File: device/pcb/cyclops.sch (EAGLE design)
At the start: 199 parts, among them Q1 NDS351AN, Q2 NDS351AN, Q3 NDS351AN, Q4 IRF510, U1 MCP4921, U10 LT1880, U11 ZXTD, U12 ADG1201, U13 THS4281, U14 ZXTD, U16 OPA1664, U2 LT1764A, U3 BD00FC0WEFJ, U4 LTM8020, U5 LT1931, U6 TPS72325, U7 TLV3701, U75 TXB0104RGYR, U8 LT1711, U9 ADR03

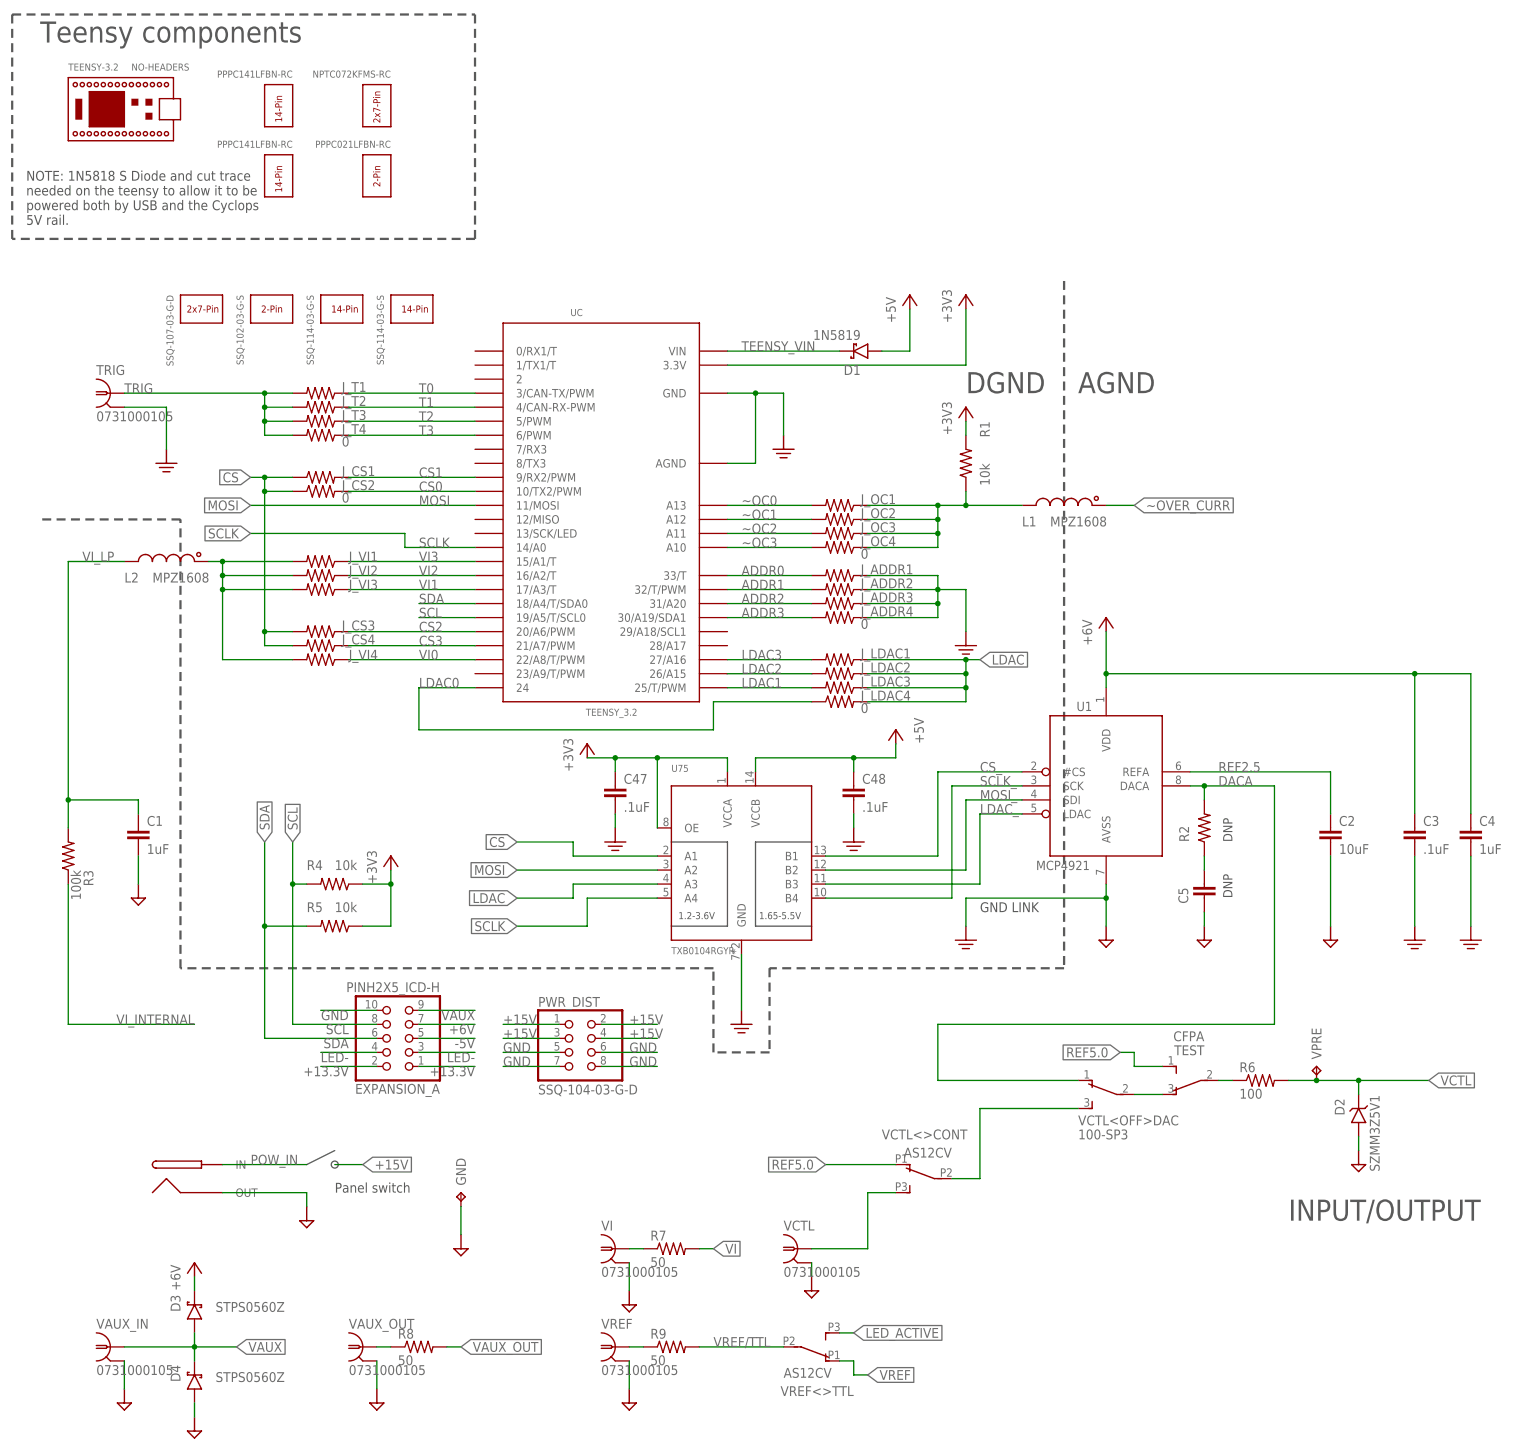
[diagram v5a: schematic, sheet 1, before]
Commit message: More pre-production fixes for Filipe.
- Better cutouts on Exapansion B in panel
- Panel alignment
- Schematic fixes (remove teensy cut trace/diode requirement)
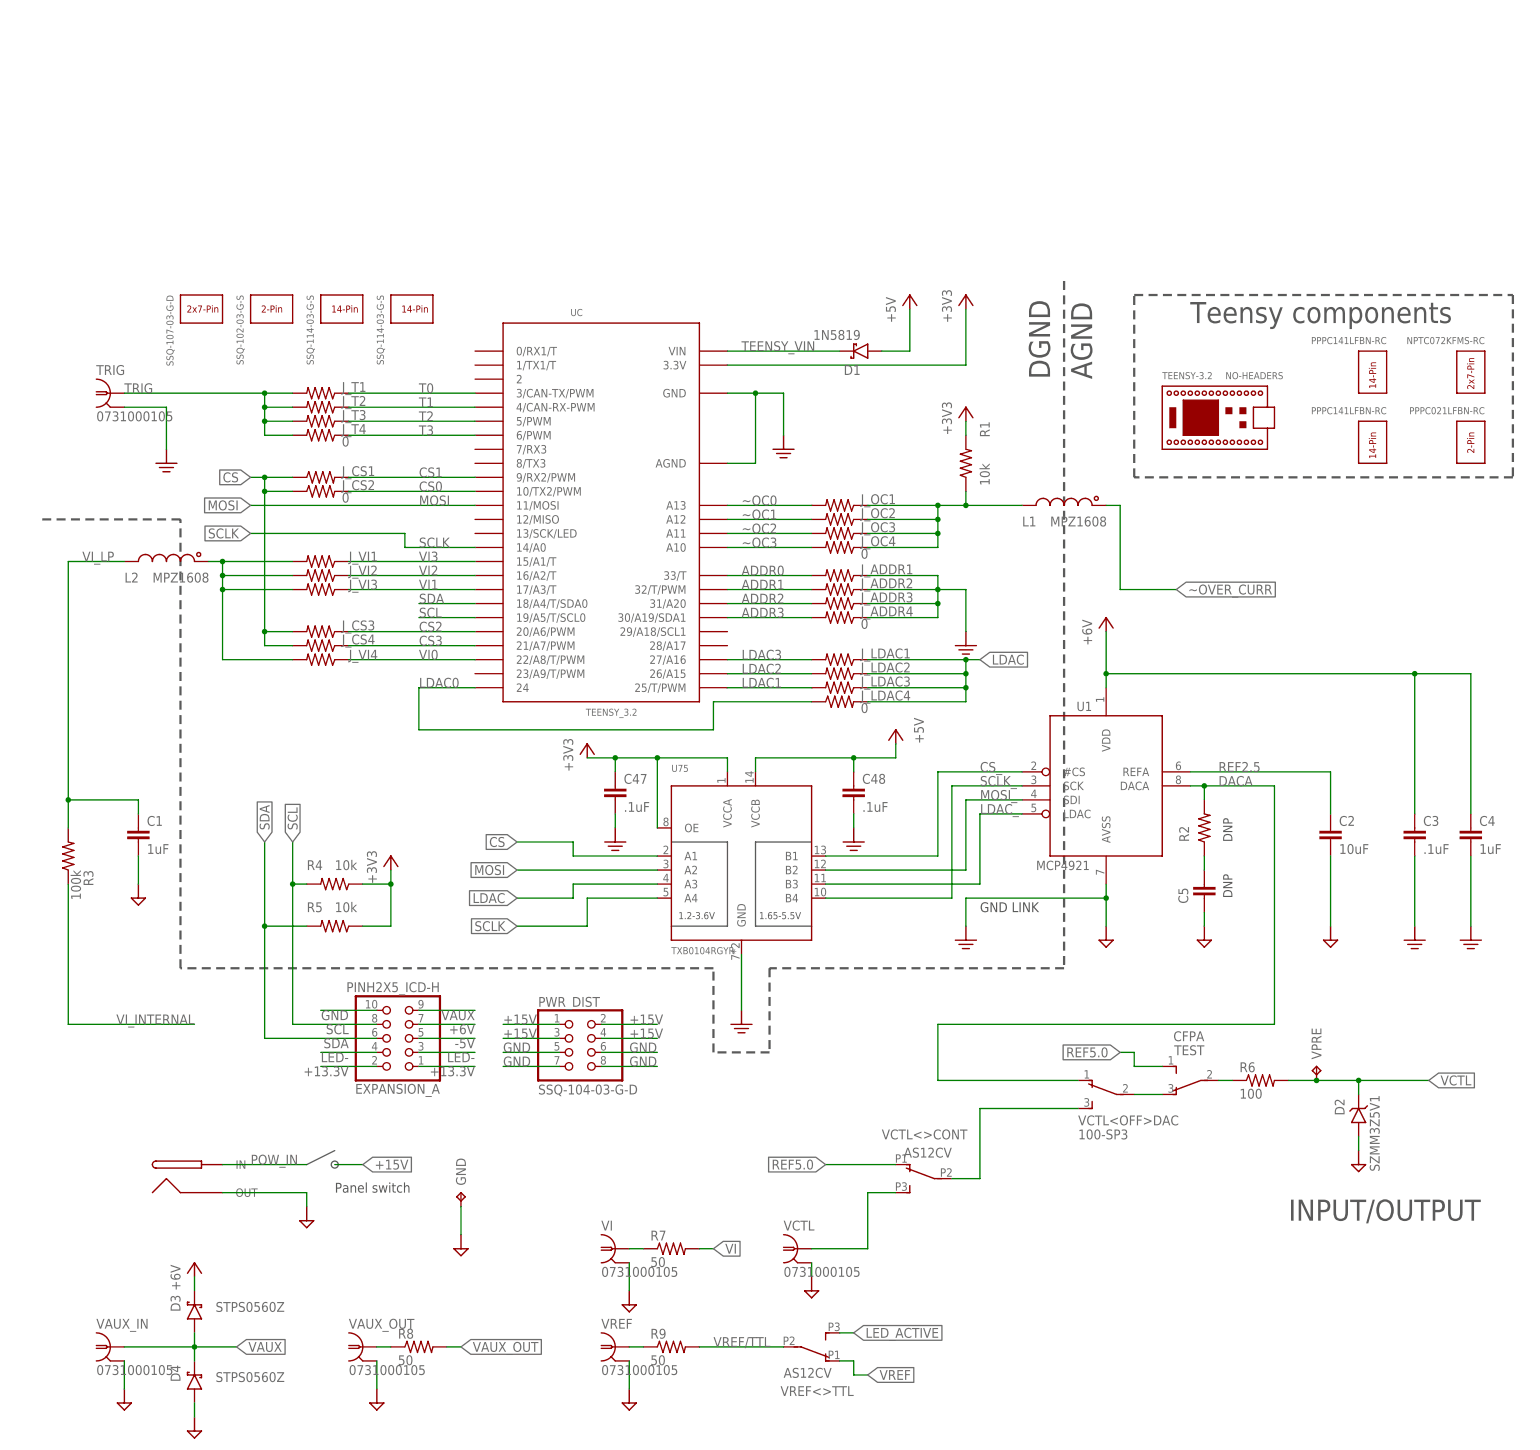
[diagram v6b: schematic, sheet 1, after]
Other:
- note removed: "NOTE: 1N5818 S Diode and cut trace needed on the teensy to allow it to be powered both by USB and the Cyclops 5V rail."
- moved on the sheet: TEENSY-3.2
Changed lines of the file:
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@@
 <wire x1="114.3" y1="2.54" x2="114.3" y2="17.78" width="0.4064" layer="97" style="shortdash"/>
 <wire x1="114.3" y1="17.78" x2="17.78" y2="17.78" width="0.4064" layer="97" style="shortdash"/>
-<text x="180.34" y="121.92" size="3.81" layer="97">AGND</text>
-<text x="160.02" y="121.92" size="3.81" layer="97">DGND</text>
+<text x="182.88" y="124.46" size="3.81" layer="97" rot="R90">AGND</text>
+<text x="175.26" y="124.46" size="3.81" layer="97" rot="R90">DGND</text>
 <wire x1="17.78" y1="17.78" x2="17.78" y2="99.06" width="0.4064" layer="97" style="shortdash"/>
 <wire x1="17.78" y1="99.06" x2="-7.62" y2="99.06" width="0.4064" layer="97" style="shortdash"/>
-<wire x1="-12.7" y1="190.5" x2="71.12" y2="190.5" width="0.4064" layer="97" style="shortdash"/>
-<wire x1="71.12" y1="190.5" x2="71.12" y2="149.86" width="0.4064" layer="97" style="shortdash"/>
-<wire x1="71.12" y1="149.86" x2="-12.7" y2="149.86" width="0.4064" layer="97" style="shortdash"/>
-<wire x1="-12.7" y1="149.86" x2="-12.7" y2="190.5" width="0.4064" layer="97" style="shortdash"/>
-<text x="-7.62" y="185.42" size="3.81" layer="97">Teensy components</text>
+<wire x1="190.5" y1="139.7" x2="259.08" y2="139.7" width="0.4064" layer="97" style="shortdash"/>
+<wire x1="259.08" y1="139.7" x2="259.08" y2="106.68" width="0.4064" layer="97" style="shortdash"/>
+<wire x1="259.08" y1="106.68" x2="190.5" y2="106.68" width="0.4064" layer="97" style="shortdash"/>
+<wire x1="190.5" y1="106.68" x2="190.5" y2="139.7" width="0.4064" layer="97" style="shortdash"/>
+<text x="200.66" y="134.62" size="3.81" layer="97">Teensy components</text>
 <text x="208.28" y="40.64" size="1.6764" layer="97" rot="R90">DNP</text>
 <text x="208.28" y="30.48" size="1.6764" layer="97" rot="R90">DNP</text>
-<text x="-10.16" y="152.4" size="1.778" layer="97">NOTE: 1N5818 S Diode and cut trace
-needed on the teensy to allow it to be
-powered both by USB and the Cyclops
-5V rail.</text>
 </plain>
 <instances>
@@
 <instance part="U$55" gate="G$1" x="43.18" y="134.62"/>
 <instance part="U$63" gate="G$1" x="55.88" y="134.62"/>
-<instance part="U$66" gate="G$1" x="50.8" y="177.8" rot="R270"/>
-<instance part="U$72" gate="G$1" x="33.02" y="177.8" rot="R270"/>
-<instance part="U$73" gate="G$1" x="33.02" y="165.1" rot="R270"/>
-<instance part="TEENSY-3.2" gate="G$1" x="-2.54" y="167.64"/>
+<instance part="U$66" gate="G$1" x="248.92" y="129.54" rot="R270"/>
+<instance part="U$72" gate="G$1" x="231.14" y="129.54" rot="R270"/>
+<instance part="U$73" gate="G$1" x="231.14" y="116.84" rot="R270"/>
+<instance part="TEENSY-3.2" gate="G$1" x="195.58" y="111.76"/>
 <instance part="J_ADDR1" gate="R" x="137.16" y="88.9" smashed="yes" rot="R180">
 <attribute name="NAME" x="140.97" y="89.1286" size="1.778" layer="95"/>
@@
 <instance part="GND" gate="G$1" x="68.58" y="-22.86"/>
 <instance part="U$79" gate="G$1" x="68.58" y="-33.02"/>
-<instance part="U$80" gate="G$1" x="50.8" y="165.1" rot="R270"/>
+<instance part="U$80" gate="G$1" x="248.92" y="116.84" rot="R270"/>
 <instance part="P+20" gate="1" x="160.02" y="119.38"/>
 <instance part="VCTL&lt;&gt;CONT" gate="G$1" x="154.94" y="-20.32" smashed="yes" rot="MR0">
@@
 <segment>
 <pinref part="L1" gate="L" pin="1"/>
-<wire x1="185.42" y1="101.6" x2="190.5" y2="101.6" width="0.1524" layer="91"/>
-<label x="190.5" y="101.6" size="1.778" layer="95" xref="yes"/>
-</segment>
-</net>
+<wire x1="185.42" y1="101.6" x2="187.96" y2="101.6" width="0.1524" layer="91"/>
+<wire x1="187.96" y1="101.6" x2="187.96" y2="86.36" width="0.1524" layer="91"/>
+<wire x1="187.96" y1="86.36" x2="198.12" y2="86.36" width="0.1524" layer="91"/>
+<label x="198.12" y="86.36" size="1.778" layer="95" xref="yes"/>
+</segment>
+</net>

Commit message: Simplification of cyclops library
- Also found that I had the OC and VI pins swiched on the Teensy pinout
(the OC pins were tied to A10-13 which are _only_ capable of analog
input). I simply swiched the pins and reflected that change in the
library. Now A10-13 are used for VI which is only analog in.
- For now, I will leave the GSOC dev stuff on its own branch and remove
it from the repo for the 3.6 production. Hopefully it can be integrated
in the future. It is too complicated and unfinished to be merged with
master right now.
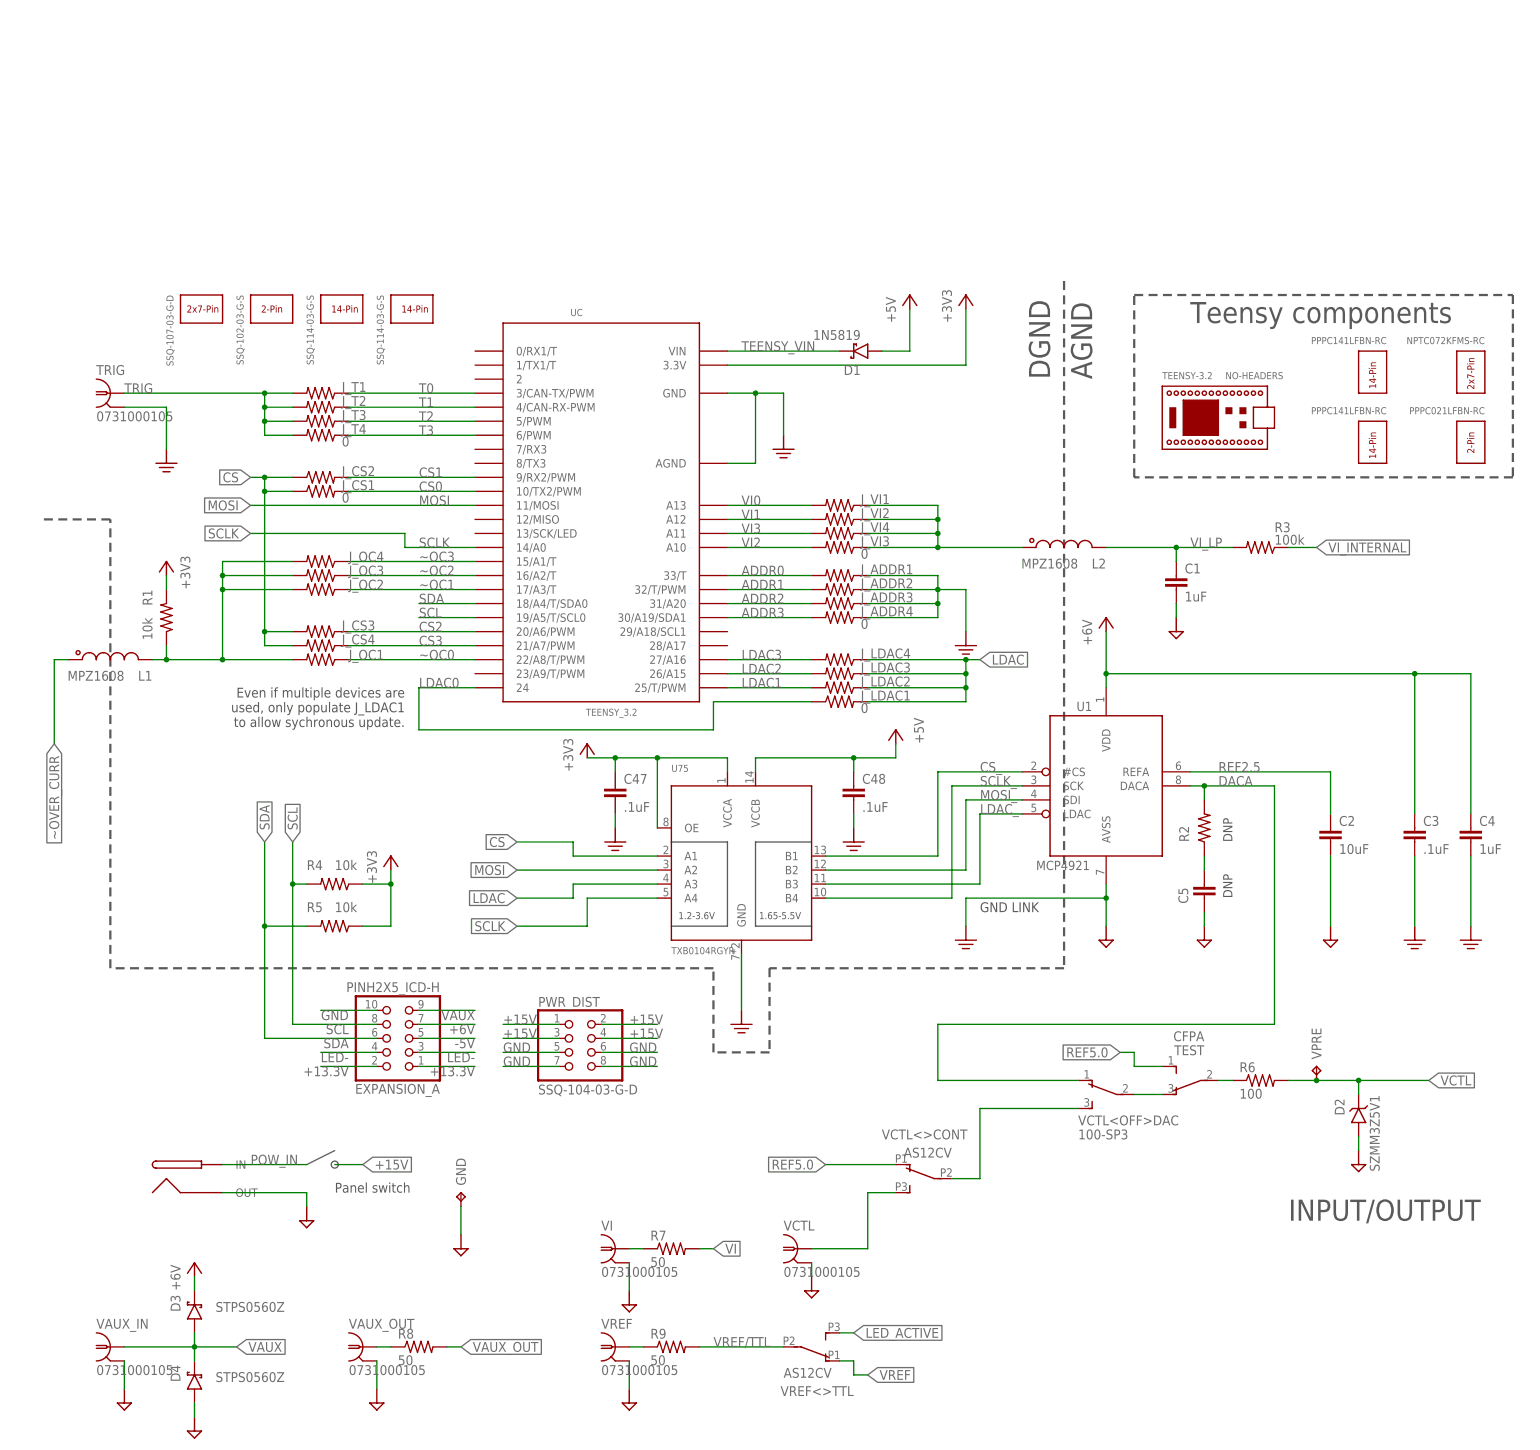
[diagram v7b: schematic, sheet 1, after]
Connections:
- removed net N$58: J_VI1.2, J_VI2.2, J_VI3.2, J_VI4.2, L2.1
- new net VI_IN: J_VI1.1, J_VI2.1, J_VI3.1, J_VI4.1, L2.1
- net CS0: now also J_CS1.2; no longer J_CS2.2
- net CS1: now also J_CS2.2; no longer J_CS1.2
- net LDAC: now also J_LDAC1.2, J_LDAC4.1; no longer J_LDAC1.1, J_LDAC4.2
- net LDAC0: now also J_LDAC1.1; no longer J_LDAC4.1
- net LDAC1: now also J_LDAC2.2; no longer J_LDAC3.2
- net LDAC2: now also J_LDAC3.2; no longer J_LDAC2.2
- net LDAC3: now also J_LDAC4.2; no longer J_LDAC1.2
- net VI0: now also J_VI1.2, UC.A13; no longer J_VI4.1, UC.22/A8/T/PWM
- net VI1: now also J_VI2.2, UC.A12; no longer J_VI3.1, UC.17/A3/T
- net VI2: now also J_VI3.2, UC.A10; no longer J_VI2.1, UC.16/A2/T
- net VI3: now also J_VI4.2, UC.A11; no longer J_VI1.1, UC.15/A1/T
- net ~OC0: now also J_OC1.1, UC.22/A8/T/PWM; no longer J_OC1.2, UC.A13
- net ~OC1: now also J_OC2.1, UC.17/A3/T; no longer J_OC2.2, UC.A12
- net ~OC2: now also J_OC3.1, UC.16/A2/T; no longer J_OC3.2, UC.A11
- net ~OC3: now also J_OC4.1, UC.15/A1/T; no longer J_OC4.2, UC.A10
- net ~OVER_CURR_PRE: now also J_OC1.2, J_OC2.2, J_OC3.2, J_OC4.2; no longer J_OC1.1, J_OC2.1, J_OC3.1, J_OC4.1
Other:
- note added: "Even if multiple devices are used, only populate J_LDAC1 to allow sychronous update."
- moved on the sheet: C1, J_CS1, J_CS2, J_LDAC1, J_LDAC2, J_LDAC3, J_LDAC4, J_OC1, J_OC2, J_OC3, J_OC4, J_VI1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
